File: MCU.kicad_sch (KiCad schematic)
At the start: 50 parts, among them U1901 ADG1607xCP, U1902 ADG1607xCP, U1903 LP38690SDX-3.3/NOPB, U1904 MSP430FR5969IRGZR, U1905 MSP430FR5969IRGZR, U1906 TCAN4551RGYRQ1

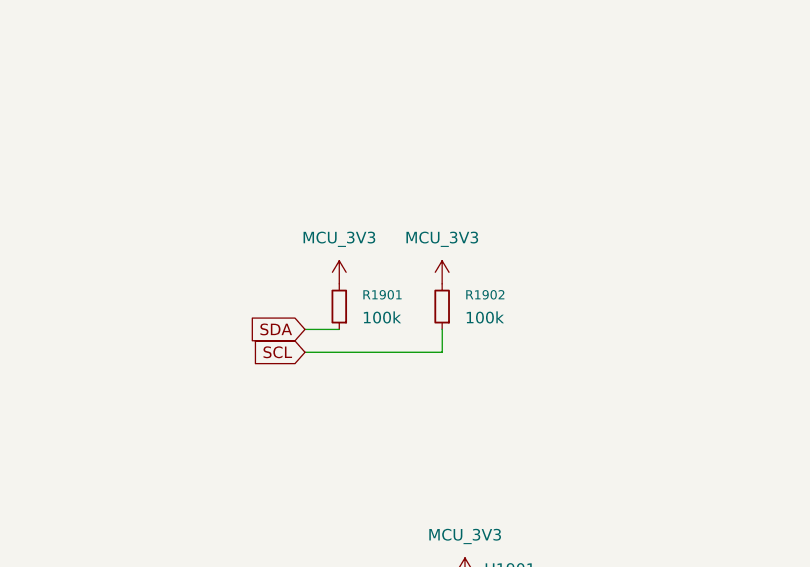
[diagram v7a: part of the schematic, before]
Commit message: deleted unused sheets, added standalone current measure sheet
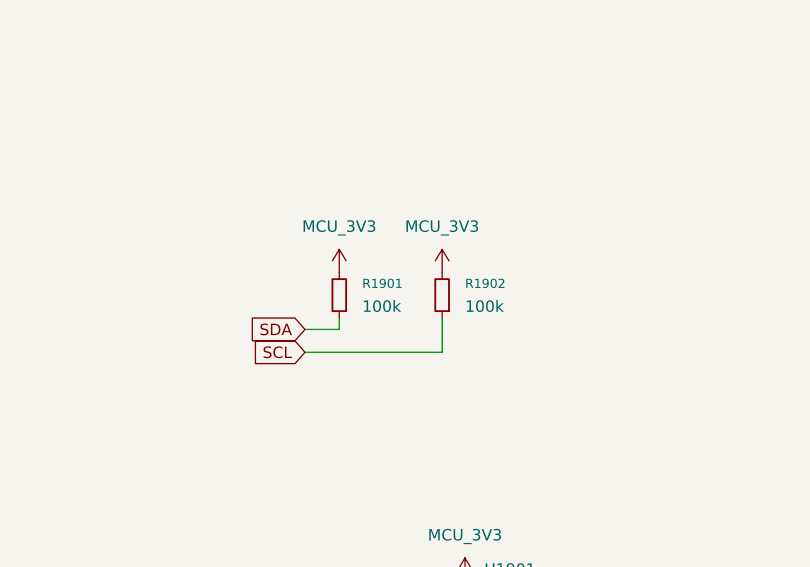
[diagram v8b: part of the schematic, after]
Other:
- sheet 5V_DCDC_1: file LDO_5V.kicad_sch -> DCDC_ADJUCTABLE.kicad_sch
- moved on the sheet: R1901, R1902
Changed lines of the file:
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@@
 	(wire
 		(pts
+			(xy 38.1 87.63) (xy 34.29 87.63)
+		)
+		(stroke
+			(width 0)
+			(type default)
+		)
+	)
+	(wire
+		(pts
 			(xy -128.27 72.39) (xy -113.03 72.39)
 		)
@@
 	(wire
 		(pts
+			(xy 38.1 86.36) (xy 38.1 87.63)
+		)
+		(stroke
+			(width 0)
+			(type default)
+		)
+	)
+	(wire
+		(pts
 			(xy -57.15 86.36) (xy -43.18 86.36)
 		)
@@
 	(wire
 		(pts
-			(xy 49.53 87.63) (xy 49.53 90.17)
+			(xy 49.53 86.36) (xy 49.53 90.17)
 		)
 		(stroke
@@
 		)
 	)
-	(wire
-		(pts
-			(xy 34.29 87.63) (xy 38.1 87.63)
-		)
-		(stroke
-			(width 0)
-			(type default)
-		)
-	)
 	(bus
 		(pts
@@
 	(symbol
 		(lib_id "Device:R_Small")
-		(at 38.1 85.09 180)
+		(at 38.1 83.82 180)
 		(unit 1)
 		(exclude_from_sim no)
@@
 		(fields_autoplaced yes)
 		(property "Reference" "R1901"
-			(at 40.64 83.8199 0)
+			(at 40.64 82.5499 0)
 			(effects
 				(font
@@
 		)
 		(property "Value" "100k"
-			(at 40.64 86.3599 0)
+			(at 40.64 85.0899 0)
 			(effects
 				(font
@@
 		)
 		(property "Footprint" "Resistor_SMD:R_0603_1608Metric_Pad0.98x0.95mm_HandSolder"
-			(at 38.1 85.09 0)
+			(at 38.1 83.82 0)
 			(effects
 				(font
@@
 		)
 		(property "Datasheet" "~"
-			(at 38.1 85.09 0)
+			(at 38.1 83.82 0)
 			(effects
 				(font
@@
 		)
 		(property "Description" "Resistor, small symbol"
-			(at 38.1 85.09 0)
+			(at 38.1 83.82 0)
 			(effects
 				(font
@@
 	(symbol
 		(lib_id "Device:R_Small")
-		(at 49.53 85.09 180)
+		(at 49.53 83.82 180)
 		(unit 1)
 		(exclude_from_sim no)
@@
 		(fields_autoplaced yes)
 		(property "Reference" "R1902"
-			(at 52.07 83.8199 0)
+			(at 52.07 82.5499 0)
 			(effects
 				(font
@@
 		)
 		(property "Value" "100k"
-			(at 52.07 86.3599 0)
+			(at 52.07 85.0899 0)
 			(effects
 				(font
@@
 		)
 		(property "Footprint" "Resistor_SMD:R_0603_1608Metric_Pad0.98x0.95mm_HandSolder"
-			(at 49.53 85.09 0)
+			(at 49.53 83.82 0)
 			(effects
 				(font
@@
 		)
 		(property "Datasheet" "~"
-			(at 49.53 85.09 0)
+			(at 49.53 83.82 0)
 			(effects
 				(font
@@
 		)
 		(property "Description" "Resistor, small symbol"
-			(at 49.53 85.09 0)
+			(at 49.53 83.82 0)
 			(effects
 				(font
@@
 	(symbol
 		(lib_id "power:VD")
-		(at 38.1 82.55 0)
+		(at 38.1 81.28 0)
 		(unit 1)
 		(exclude_from_sim no)
@@
 		(fields_autoplaced yes)
 		(property "Reference" "#PWR01902"
-			(at 38.1 86.36 0)
+			(at 38.1 85.09 0)
 			(effects
 				(font
@@
 		)
 		(property "Value" "MCU_3V3"
-			(at 38.1 77.47 0)
+			(at 38.1 76.2 0)
 			(effects
 				(font
@@
 		)
 		(property "Footprint" ""
-			(at 38.1 82.55 0)
+			(at 38.1 81.28 0)
 			(effects
 				(font
@@
 		)
 		(property "Datasheet" ""
-			(at 38.1 82.55 0)
+			(at 38.1 81.28 0)
 			(effects
 				(font
@@
 		)
 		(property "Description" "Power symbol creates a global label with name \"VD\""
-			(at 38.1 82.55 0)
+			(at 38.1 81.28 0)
 			(effects
 				(font
@@
 	(symbol
 		(lib_id "power:VD")
-		(at 49.53 82.55 0)
+		(at 49.53 81.28 0)
 		(unit 1)
 		(exclude_from_sim no)
@@
 		(fields_autoplaced yes)
 		(property "Reference" "#PWR01904"
-			(at 49.53 86.36 0)
+			(at 49.53 85.09 0)
 			(effects
 				(font
@@
 		)
 		(property "Value" "MCU_3V3"
-			(at 49.53 77.47 0)
+			(at 49.53 76.2 0)
 			(effects
 				(font
@@
 		)
 		(property "Footprint" ""
-			(at 49.53 82.55 0)
+			(at 49.53 81.28 0)
 			(effects
 				(font
@@
 		)
 		(property "Datasheet" ""
-			(at 49.53 82.55 0)
+			(at 49.53 81.28 0)
 			(effects
 				(font
@@
 		)
 		(property "Description" "Power symbol creates a global label with name \"VD\""
-			(at 49.53 82.55 0)
+			(at 49.53 81.28 0)
 			(effects
 				(font
@@
 			)
 		)
-		(property "Sheetfile" "LDO_5V.kicad_sch"
+		(property "Sheetfile" "DCDC_ADJUCTABLE.kicad_sch"
 			(at 22.86 32.3346 0)
 			(effects
